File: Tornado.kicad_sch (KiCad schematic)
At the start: 42 parts, among them J1 MOLEX, J2 PWR, J3 CANH, J4 CANL, J5 GND, SW1 ID, U1 AP63205WU, U2 STM32G431KBUx, U3 LSM6DSV, U4 AP2112K-3.3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

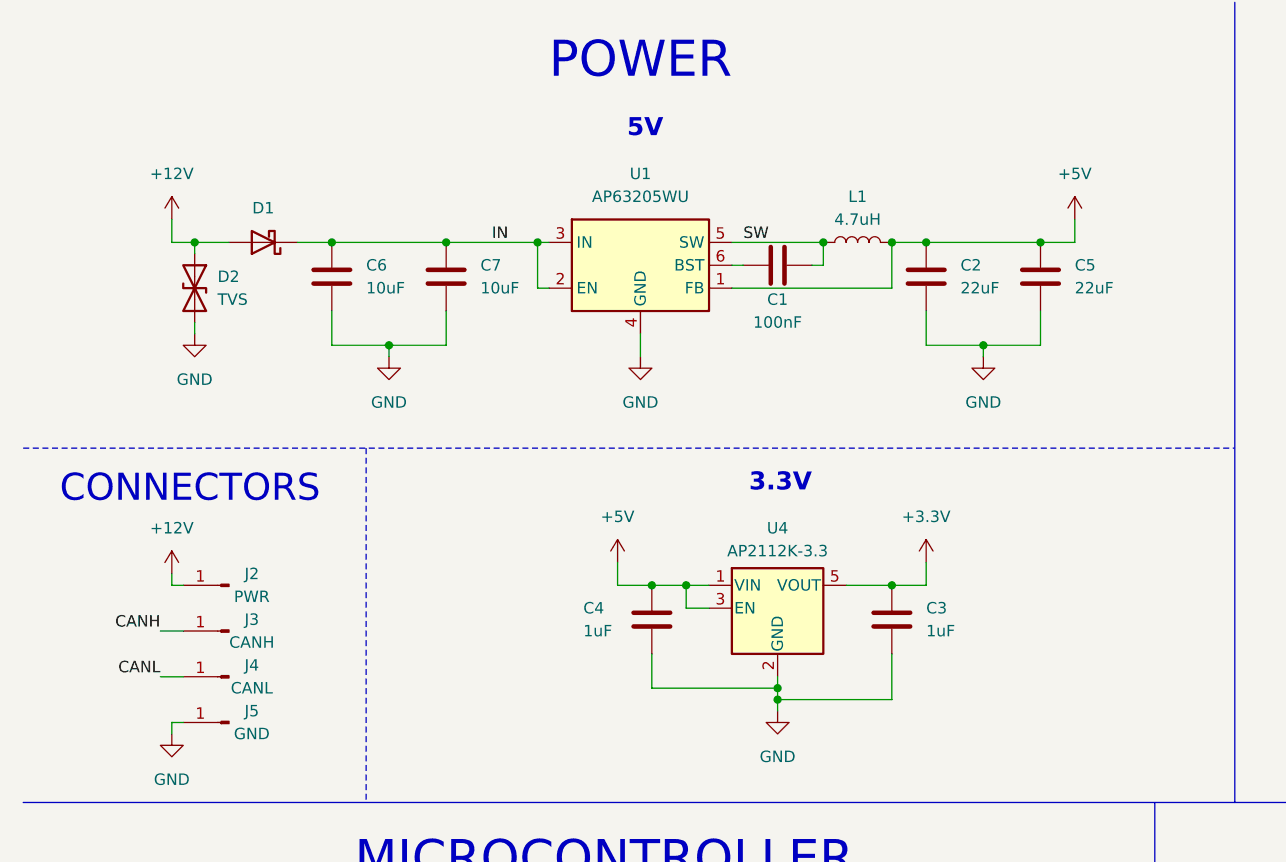
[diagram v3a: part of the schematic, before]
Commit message: Added Ferrite Bead
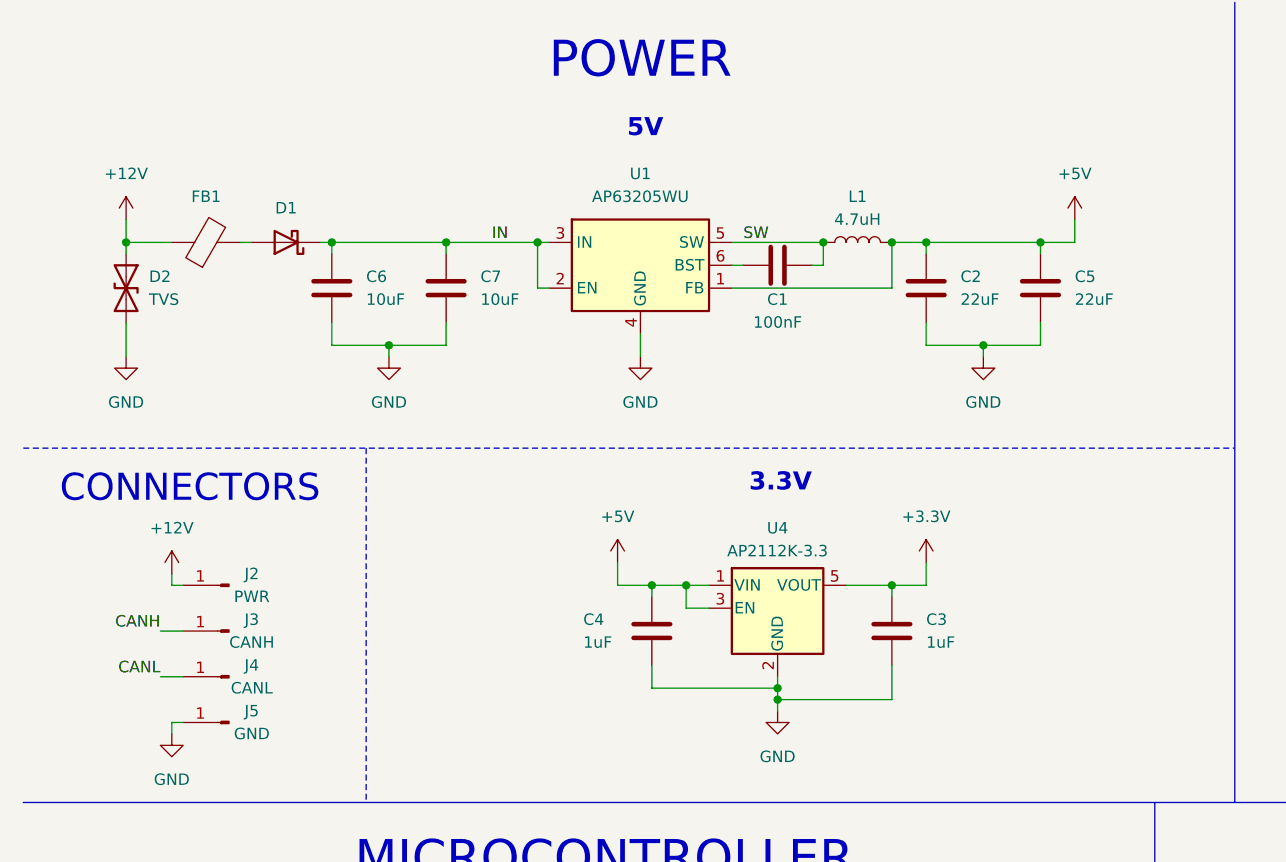
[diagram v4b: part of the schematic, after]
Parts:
- added FB1: FerriteBead, Inductor_SMD:L_0603_1608Metric, symbol Device:FerriteBead
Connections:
- net +12V: now also FB1.1; no longer D1.2 (A)
- new net: D1.2 (A), FB1.2
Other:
- moved on the sheet: C2, C3, C4, C5, C6, C7, D1, D2

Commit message: Updated RGB Symbol
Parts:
- D3, D4: symbol RGB_LED:WS2812B -> Tornado_Symbols:WS2812B_2020
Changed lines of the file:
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@@
     )
   )
-  (symbol (lib_id "RGB_LED:WS2812B") (at 167.64 40.64 0) (unit 1)
+  (symbol (lib_id "Tornado_Symbols:WS2812B_2020") (at 167.64 40.64 0) (unit 1)
     (in_bom yes) (on_board yes) (dnp no)
     (property "Reference" "D3" (at 177.8 34.29 0)
@@
     )
   )
-  (symbol (lib_id "RGB_LED:WS2812B") (at 190.5 40.64 0) (unit 1)
+  (symbol (lib_id "Tornado_Symbols:WS2812B_2020") (at 190.5 40.64 0) (unit 1)
     (in_bom yes) (on_board yes) (dnp no)
     (property "Reference" "D4" (at 200.66 34.29 0)

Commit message: Added resistor to filter
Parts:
- removed FB1: FerriteBead, Inductor_SMD:L_0603_1608Metric, symbol Device:FerriteBead
- added R4: 5, Resistor_SMD:R_0603_1608Metric, symbol Device:R
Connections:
- net +12V: now also R4.2
- net at D1.2 (A): now also R4.1
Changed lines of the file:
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@@
-    )
-  )
-  (symbol (lib_id "Device:FerriteBead") (at 33.02 39.37 90) (unit 1)
-    (in_bom yes) (on_board yes) (dnp no)
-    (property "Reference" "FB1" (at 33.02 34.29 90)
-      (effects (font (size 1.27 1.27)))
-    )
-    (property "Value" "FerriteBead" (at 32.9692 34.29 90)
-      (effects (font (size 1.27 1.27)) hide)
-    )
-    (property "Footprint" "Inductor_SMD:L_0603_1608Metric" (at 33.02 41.148 90)
-      (effects (font (size 1.27 1.27)) hide)
-    )
-    (property "Datasheet" "~" (at 33.02 39.37 0)
-      (effects (font (size 1.27 1.27)) hide)
-    )
-    (pin "2")
-    (pin "1")
-    (instances
-      (project "Tornado"
-        (path "/74d9931a-8786-4de9-b7a7-1d1158c87647"
-          (reference "FB1") (unit 1)
-        )
-      )
     )
   )
@@
         )
       )
+    )
+  )
+  (symbol (lib_id "Device:R") (at 33.02 39.37 270) (unit 1)
+    (in_bom yes) (on_board yes) (dnp no)
+    (property "Reference" "R4" (at 31.75 34.29 90)
+      (effects (font (size 1.27 1.27)) (justify left))
+    )
+    (property "Value" "5" (at 31.75 36.83 90)
+      (effects (font (size 1.27 1.27)) (justify left))
+    )
+    (property "Footprint" "Resistor_SMD:R_0603_1608Metric" (at 33.02 37.592 90)
+      (effects (font (size 1.27 1.27)) hide)
+    )
+    (property "Datasheet" "~" (at 33.02 39.37 0)
+      (effects (font (size 1.27 1.27)) hide)
+    )
+    (pin "1")
+    (pin "2")
+    (instances
+      (project "Tornado"
+        (path "/74d9931a-8786-4de9-b7a7-1d1158c87647"
+          (reference "R4") (unit 1)
+        )
+      )
